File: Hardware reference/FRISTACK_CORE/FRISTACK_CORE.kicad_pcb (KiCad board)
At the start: 2 copper layers, 51 x 51 mm, 77 parts, among them J1 USB_C_Receptacle_USB2.0_16P, J3 Conn_01x02_Pin, J4 Conn_01x13_Socket, J5 Conn_01x13_Socket, J6 Conn_01x02_Pin, U1 AZ1117-3.3, U2 USBLC6-2SC6, U3 ESP32-S3-MINI-1U, U4 FUSB42, U5 SN65HVD232, Y1 32.768 kHz

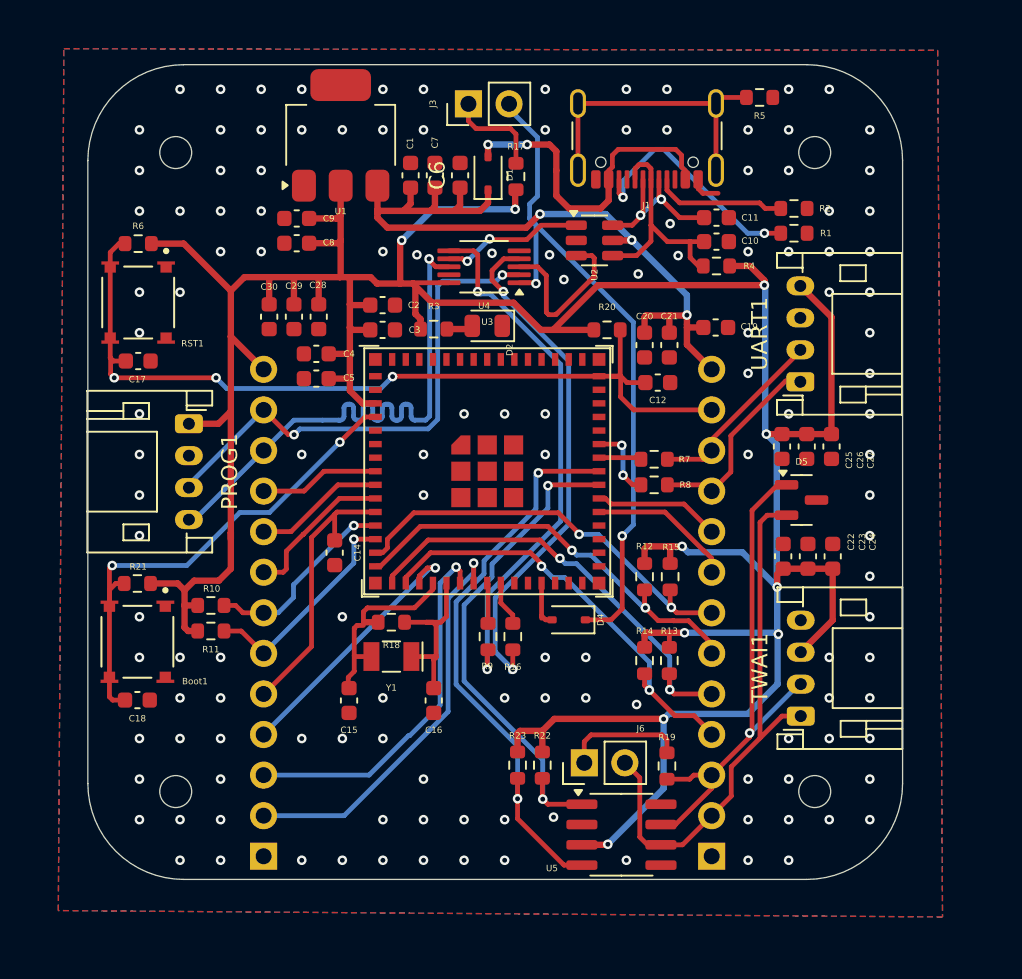
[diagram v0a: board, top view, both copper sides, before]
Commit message: Power management changes on CORE and SENSOR_NODE
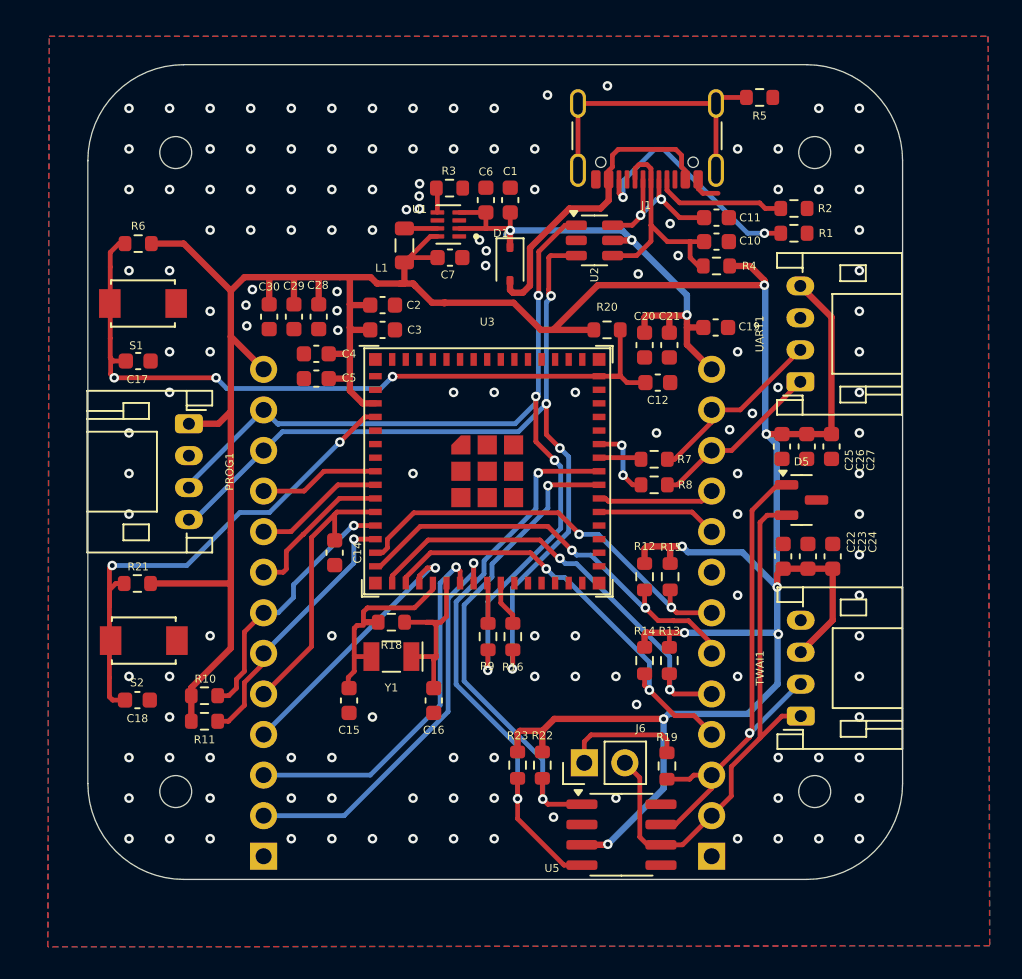
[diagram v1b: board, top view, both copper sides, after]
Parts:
- removed Boot1, RST1: TL3315NF100Q, User_imports:SW_TL3315NF100Q
- removed C8: 0.1uF, Capacitor_SMD:C_0603_1608Metric
- removed C9: 10uF, Capacitor_SMD:C_0603_1608Metric
- removed D2: LED RED, LED_SMD:LED_0805_2012Metric
- removed D4: 1N5819WS, Diode_SMD:D_SOD-323
- removed J3: Conn_01x02_Pin, Connector_PinHeader_2.54mm:PinHeader_1x02_P2.54mm_Vertical
- removed R17: 10K, Resistor_SMD:R_0603_1608Metric
- removed U4: FUSB42, Package_SO:VSSOP-10_3x3mm_P0.5mm
- added L1: 2.2uH, Inductor_SMD:L_0805_2012Metric, F.Cu at (146.8, 83.3)
- added S1: TS-1088-AR02016, User_imports:SW_TS-1088-AR02016, F.Cu at (130.4, 87.0)
- added S2: TS-1088-AR02016, User_imports:SW_TS-1088-AR02016, F.Cu at (130.5, 108.0)
- C6: value 10uF -> 4.7uF
- C7: value 0.1uF -> 10uF
- R3: value 75 -> 267k
- U1: value AZ1117-3.3 -> TPS62840DLCR; footprint Package_TO_SOT_SMD:SOT-223 -> User_imports:SON50P200X150X100-8N
- moved R3 8.88 mm to (149.6, 79.7)
- moved U1 8.75 mm to (149.6, 82.0), turned to 180 degrees
- moved C1 6.43 mm to (153.4, 80.5)
- moved D1 5.84 mm to (153.4, 84.5), turned to -90 degrees
- moved R10 5.66 mm to (134.3, 111.5)
- moved R11 5.66 mm to (134.3, 113.1)
- moved C7 5.24 mm to (149.7, 84.1), turned to 0 degrees
- moved C6 2.24 mm to (151.9, 80.5)
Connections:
- C7 pad 1: +5V -> ESP_PWR
- J4 pad 11: USB_P_HD -> USB_P_2
- J4 pad 12: USB_N_HD -> USB_N_2
- J5 pad 10: UART0_RX -> BOOT
- J5 pad 11: UART0_TX -> UART0_RX
- J5 pad 12: EN -> UART0_TX
- J5 pad 9: GPIO40 -> RST
- PROG1 pad 3: USB_N_HD -> USB_N_2
- PROG1 pad 4: USB_P_HD -> USB_P_2
- R16 pad 2: USB_P_ESP -> USB_P_2
- R3 pad 1: ESP_PWR -> Net-(U1-VSET)
- R3 pad 2: Net-(D2-A) -> GND
- R9 pad 2: USB_N_ESP -> USB_N_2
- U1 pad 2: ESP_PWR -> +5V
- U1 pad 3: +5V -> GND
- U1 pad 4: (no net) -> +5V
- U3 pad 27: GPIO47 -> unconnected-(U3-IO47-Pad27)
- U3 pad 35: GPIO39 -> RST
- U3 pad 36: GPIO40 -> BOOT
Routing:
- net USB_N_2: track 9.17 -> 58.7 mm, vias 2 -> 4
- net USB_P_2: track 10.6 -> 56.3 mm, vias 0 -> 4
- net Net-(D4-K): track 42.9 -> 0.00 mm, vias 2 -> 0
- net USB_P_HD: track 34.8 -> 0.00 mm, vias 1 -> 0
- net USB_N_ESP: track 33.5 -> 0.00 mm, vias 2 -> 0
- net USB_P_ESP: track 32.8 -> 0.00 mm, vias 2 -> 0
- net USB_N_HD: track 32.7 -> 0.00 mm, vias 2 -> 0
- net +5V: track 49.1 -> 33.5 mm
- net ESP_PWR: track 232.1 -> 217.0 mm, vias 10 -> 8
- net GPIO39: track 9.12 -> 0.00 mm
- net GPIO40: track 7.91 -> 0.00 mm
- net RST: track 0.00 -> 7.56 mm
- net BOOT: track 0.00 -> 7.39 mm
- net EN: track 55.1 -> 47.8 mm
- net Net-(J3-Pin_1): track 6.22 -> 0.00 mm
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
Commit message: Added logos, annotations
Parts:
- added D2: 1N5819WS, Diode_SMD:D_SOD-323, F.Cu at (154.0, 77.0)
- added G***: LOGO, User_imports:fri_logo, B.Cu at (151.9, 83.8)
- added G***: LOGO, User_imports:lead_free, B.Cu at (131.4, 111.1)
- added J2: JTAG_PIN_HEADER, Connector_PinHeader_2.54mm:PinHeader_1x02_P2.54mm_Vertical, F.Cu at (158.1, 108.6)
- added J3: BAT, Connector_JST:JST_PH_S2B-PH-K_1x02_P2.00mm_Horizontal, F.Cu at (144.4, 78.4)
- C6, C7: footprint Capacitor_SMD:C_0603_1608Metric -> Capacitor_SMD:C_0402_1005Metric
- L1: footprint Inductor_SMD:L_0805_2012Metric -> User imports:INDC2016X120N
- R18: value ? -> 1M
- moved L1 0.42 mm to (146.8, 83.7)
- moved C6 0.28 mm to (151.9, 80.8)
- renumbered S2 to BOOT, S1 to RST, TWAI1 to TWAI0, UART1 to UART0
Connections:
- J5 pad 8: GPIO39 -> GND
- TWAI0 pad 3: ESP_PWR -> GND
- TWAI0 pad 4: GND -> ESP_PWR
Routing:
- net Net-(D2-K): track 0.00 -> 9.15 mm
- net CAN_R: track 35.7 -> 43.5 mm, vias 2 -> 3
- net +5V: track 33.5 -> 40.7 mm
- net CAN_D: track 31.0 -> 36.4 mm
- net ESP_PWR: track 217.0 -> 215.0 mm
- net GND: track 2.73 -> 3.45 mm, vias 140 -> 131
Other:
- board text added: "+5V"
- board text added: "ADC_1/IO7"
- board text added: "BOOT/IO40/TDO"
- board text added: "CAN_D/IO41/TDI"
- board text added: "CAN_H"
- board text added: "CAN_L"
- board text added: "CAN_R/IO42/TMS"
- board text added: "CS/IO10"
- board text added: "ESP_PWR"
- board text added: "GND"
- board text added: "GPIO14"
- board text added: "GPIO17"
- board text added: "GPIO18"
- board text added: "I2S_DIN/IO5"
- board text added: "I2S_DOUT/IO6"
- board text added: "I2S_LRCK/IO4"
- board text added: "MISO/IO11"
- board text added: "MOSI/IO13"
- board text added: "RST/IO39/TCK"
- board text added: "SCK/IO12"
- board text added: "SCL/IO9"
- board text added: "SDA/IO8"
- board text added: "UART0_RX"
- board text added: "UART0_TX"
- board text added: "USB_N"
- board text added: "USB_P"

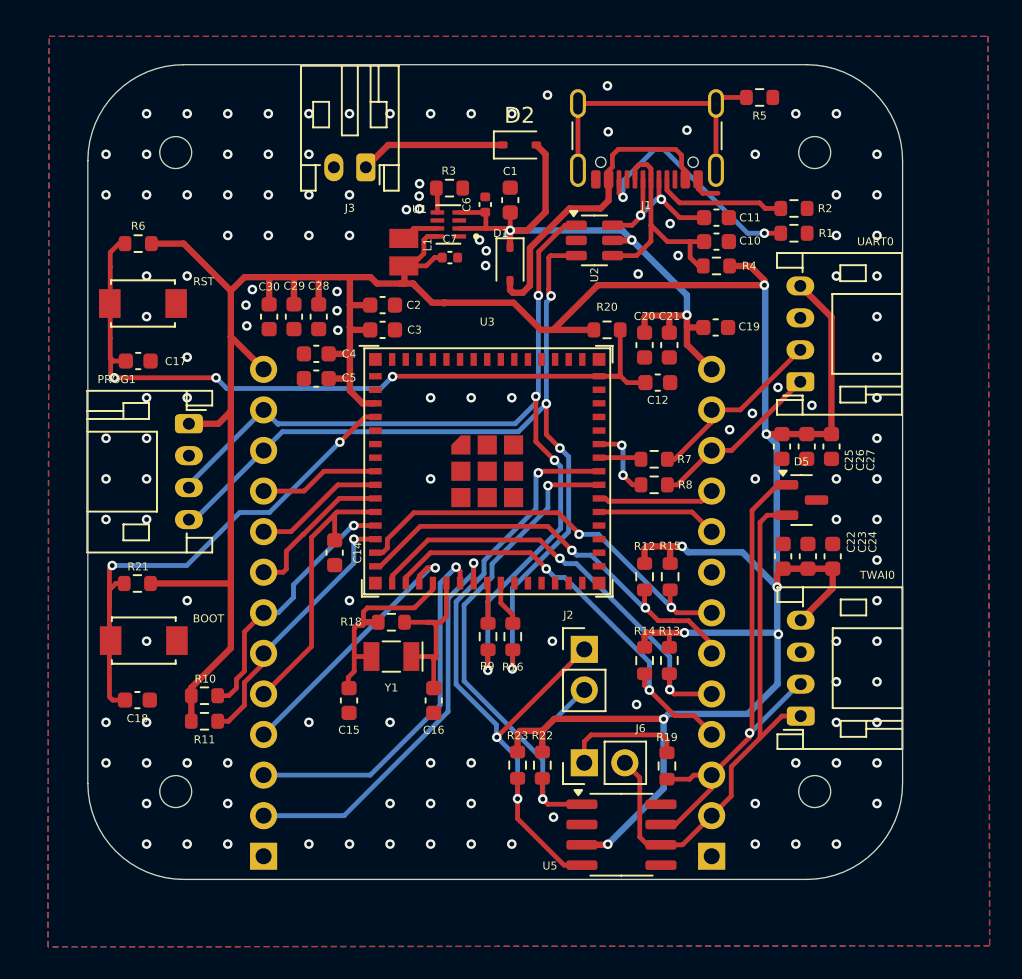
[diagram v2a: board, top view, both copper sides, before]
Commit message: Added USBSwitch to Core and added first version of Compatibility
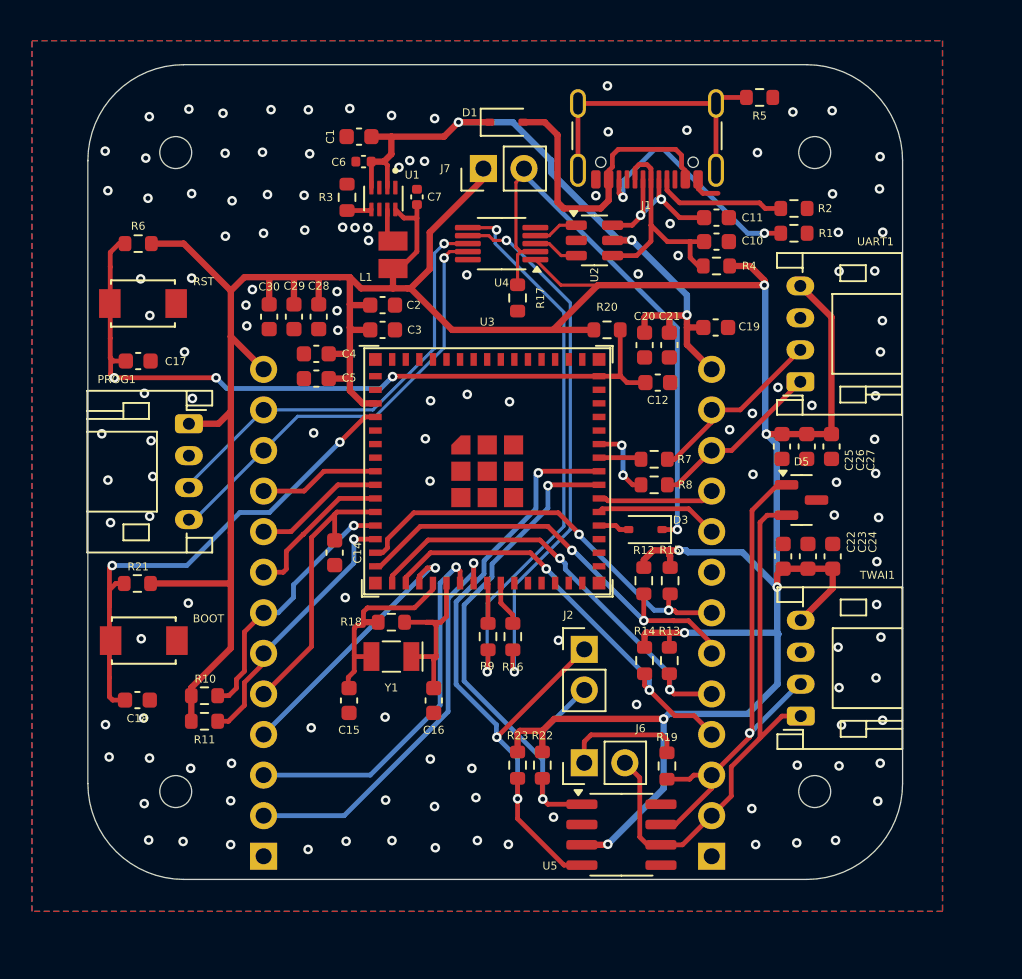
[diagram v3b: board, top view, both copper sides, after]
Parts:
- removed D2: 1N5819WS, Diode_SMD:D_SOD-323
- removed J3: BAT, Connector_JST:JST_PH_S2B-PH-K_1x02_P2.00mm_Horizontal
- added D3: 1N5819WS, Diode_SMD:D_SOD-323, F.Cu at (161.9, 101.1)
- added J7: Conn_01x02_Pin, Connector_PinHeader_2.54mm:PinHeader_1x02_P2.54mm_Vertical, F.Cu at (151.8, 78.5)
- added R17: 10K, Resistor_SMD:R_0603_1608Metric, F.Cu at (153.9, 86.6)
- added U4: FSUSB42MUX, Package_SO:MSOP-10_3x3mm_P0.5mm, F.Cu at (152.9, 83.2)
- moved C1 10.3 mm to (144.0, 76.5), turned to 180 degrees
- moved D1 8.88 mm to (153.2, 75.6), turned to 0 degrees
- moved C6 8.08 mm to (144.3, 78.1), turned to 180 degrees
- moved R3 6.44 mm to (143.2, 80.3), turned to 90 degrees
- moved U1 4.38 mm to (145.5, 80.4), turned to -90 degrees
- moved C7 4.32 mm to (147.6, 80.3), turned to 90 degrees
- moved L1 0.69 mm to (146.1, 83.9)
- moved R12 0.25 mm to (161.8, 104.3)
- moved R15 0.25 mm to (163.4, 104.3)
- renumbered TWAI0 to TWAI1, UART0 to UART1
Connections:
- J4 pad 11: USB_P_2 -> USB_P_HD
- J4 pad 12: USB_N_2 -> USB_N_HD
- PROG1 pad 3: USB_N_2 -> USB_N_HD
- PROG1 pad 4: USB_P_2 -> USB_P_HD
- R16 pad 2: USB_P_2 -> USB_P_ESP
- R9 pad 2: USB_N_2 -> USB_N_ESP
- U3 pad 34: unconnected-(U3-IO38-Pad34) -> Net-(D3-A)
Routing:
- net USB_N_2: track 58.7 -> 2.83 mm, vias 4 -> 0
- net USB_P_2: track 56.3 -> 2.87 mm, vias 4 -> 0
- net SEL: track 0.00 -> 36.3 mm, vias 0 -> 1
- net USB_N_ESP: track 0.00 -> 34.8 mm, vias 0 -> 2
- net USB_P_ESP: track 0.00 -> 34.1 mm, vias 0 -> 2
- net USB_P_HD: track 0.00 -> 27.7 mm, vias 0 -> 1
- net USB_N_HD: track 0.00 -> 27.6 mm, vias 0 -> 1
- net ESP_PWR: track 215.0 -> 228.7 mm, vias 8 -> 7
- net Net-(D2-K): track 9.15 -> 0.00 mm
- net +5V: track 40.7 -> 45.2 mm
- net Net-(D3-A): track 0.00 -> 1.95 mm
- net MISO: track 27.1 -> 27.7 mm
- net GND: vias 131 -> 130
